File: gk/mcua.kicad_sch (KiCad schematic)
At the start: 16 parts, among them SW1 SW_Push, SW2 SW_Push, U4 STM32H747BITx, Y1 16MHz

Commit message: Update pcb
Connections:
- net SPKR_VOLUME: now also U4.45 (PA0); no longer U4.57 (PA4)
- net CTP_NRESET: now reaches U4.10 (PC13)
- net CTP_INT: now reaches U4.11 (PC14)
- net LED_BACKLIGHT_PWM: now reaches U4.149 (PA11)
- net SDMMC_DETECT: now reaches U4.166 (PA15)
- no-connect marks 26 -> 22
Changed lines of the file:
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@@
   (no_connect (at 68.58 146.05))
   (no_connect (at 71.12 146.05))
-  (no_connect (at 73.66 49.53))
-  (no_connect (at 35.56 49.53))
   (no_connect (at 99.06 146.05))
   (no_connect (at 139.7 49.53))
+  (no_connect (at 45.72 49.53))
   (no_connect (at 175.26 49.53))
   (no_connect (at 172.72 49.53))
@@
   (no_connect (at 165.1 146.05))
   (no_connect (at 63.5 146.05))
-  (no_connect (at 154.94 49.53))
   (no_connect (at 66.04 146.05))
-  (no_connect (at 63.5 49.53))
-  (no_connect (at 157.48 49.53))
   (no_connect (at 50.8 146.05))
   (no_connect (at 160.02 49.53))
@@
     )
   )
+  (global_label "CTP_INT" (shape input) (at 157.48 49.53 90) (fields_autoplaced)
+    (effects (font (size 1.27 1.27)) (justify left))
+    (property "Intersheetrefs" "${INTERSHEET_REFS}" (at 157.48 39.2461 90)
+      (effects (font (size 1.27 1.27)) (justify left) hide)
+    )
+  )
   (global_label "WIFI_CHIP_EN" (shape input) (at 195.58 49.53 90) (fields_autoplaced)
     (effects (font (size 1.27 1.27)) (justify left))
@@
     )
   )
+  (global_label "LED_BACKLIGHT_PWM" (shape input) (at 63.5 49.53 90) (fields_autoplaced)
+    (effects (font (size 1.27 1.27)) (justify left))
+    (property "Intersheetrefs" "${INTERSHEET_REFS}" (at 63.5 26.9695 90)
+      (effects (font (size 1.27 1.27)) (justify left) hide)
+    )
+  )
   (global_label "PCM_FMT" (shape input) (at 88.9 146.05 270) (fields_autoplaced)
     (effects (font (size 1.27 1.27)) (justify right))
@@
     )
   )
-  (global_label "SPKR_VOLUME" (shape input) (at 45.72 49.53 90) (fields_autoplaced)
-    (effects (font (size 1.27 1.27)) (justify left))
-    (property "Intersheetrefs" "${INTERSHEET_REFS}" (at 45.72 33.259 90)
-      (effects (font (size 1.27 1.27)) (justify left) hide)
-    )
-  )
   (global_label "FMC_BA1" (shape input) (at 170.18 146.05 270) (fields_autoplaced)
     (effects (font (size 1.27 1.27)) (justify right))
@@
     )
   )
+  (global_label "CTP_NRESET" (shape input) (at 154.94 49.53 90) (fields_autoplaced)
+    (effects (font (size 1.27 1.27)) (justify left))
+    (property "Intersheetrefs" "${INTERSHEET_REFS}" (at 154.94 35.0734 90)
+      (effects (font (size 1.27 1.27)) (justify left) hide)
+    )
+  )
   (global_label "LTDC_HYSNC" (shape input) (at 104.14 146.05 270) (fields_autoplaced)
     (effects (font (size 1.27 1.27)) (justify right))
@@
       (effects (font (size 1.27 1.27)) (justify left) hide)
     )
+  )
+  (global_label "SPKR_VOLUME" (shape input) (at 35.56 49.53 90) (fields_autoplaced)
+    (effects (font (size 1.27 1.27)) (justify left))
+    (property "Intersheetrefs" "${INTERSHEET_REFS}" (at 35.56 33.259 90)
+      (effects (font (size 1.27 1.27)) (justify left) hide)
+    )
+  )
+  (global_label "SDMMC_DETECT" (shape input) (at 73.66 49.53 90) (fields_autoplaced)
+    (effects (font (size 1.27 1.27)) (justify left))
+    (property "Intersheetrefs" "${INTERSHEET_REFS}" (at 73.66 32.2311 90)
+      (effects (font (size 1.27 1.27)) (justify left) hide)
+    )

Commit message: Update pcb
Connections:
- net LSM6DSL_INT2 is gone; now on net WIFI_IRQ: U4.162 (PI1)
- net WIFI_IRQ: no longer U4.2 (PE3)
- net NTC_MCU: now reaches U4.60 (PA7)
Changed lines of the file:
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@@
   (no_connect (at 99.06 146.05))
   (no_connect (at 139.7 49.53))
+  (no_connect (at 215.9 49.53))
   (no_connect (at 45.72 49.53))
   (no_connect (at 175.26 49.53))
@@
   (no_connect (at 60.96 146.05))
   (no_connect (at 182.88 49.53))
-  (no_connect (at 53.34 49.53))
   (no_connect (at 137.16 49.53))
   (no_connect (at 177.8 49.53))
@@
     )
   )
-  (global_label "WIFI_IRQ" (shape input) (at 215.9 49.53 90) (fields_autoplaced)
-    (effects (font (size 1.27 1.27)) (justify left))
-    (property "Intersheetrefs" "${INTERSHEET_REFS}" (at 215.9 38.7017 90)
-      (effects (font (size 1.27 1.27)) (justify left) hide)
-    )
-  )
   (global_label "BTN_MCU_R" (shape input) (at 129.54 146.05 270) (fields_autoplaced)
     (effects (font (size 1.27 1.27)) (justify right))
@@
     )
   )
-  (global_label "LSM6DSL_INT2" (shape input) (at 81.28 146.05 270) (fields_autoplaced)
-    (effects (font (size 1.27 1.27)) (justify right))
-    (property "Intersheetrefs" "${INTERSHEET_REFS}" (at 81.28 162.4419 90)
-      (effects (font (size 1.27 1.27)) (justify right) hide)
-    )
-  )
   (global_label "VDD12" (shape input) (at 27.94 85.09 180) (fields_autoplaced)
     (effects (font (size 1.27 1.27)) (justify right))
@@
     )
   )
+  (global_label "NTC_MCU" (shape input) (at 53.34 49.53 90) (fields_autoplaced)
+    (effects (font (size 1.27 1.27)) (justify left))
+    (property "Intersheetrefs" "${INTERSHEET_REFS}" (at 53.34 38.0366 90)
+      (effects (font (size 1.27 1.27)) (justify left) hide)
+    )
+  )
   (global_label "FMC_A12" (shape input) (at 162.56 146.05 270) (fields_autoplaced)
     (effects (font (size 1.27 1.27)) (justify right))
@@
     )
   )
+  (global_label "WIFI_IRQ" (shape input) (at 81.28 146.05 270) (fields_autoplaced)
+    (effects (font (size 1.27 1.27)) (justify right))
+    (property "Intersheetrefs" "${INTERSHEET_REFS}" (at 81.28 156.8783 90)
+      (effects (font (size 1.27 1.27)) (justify right) hide)
+    )
+  )

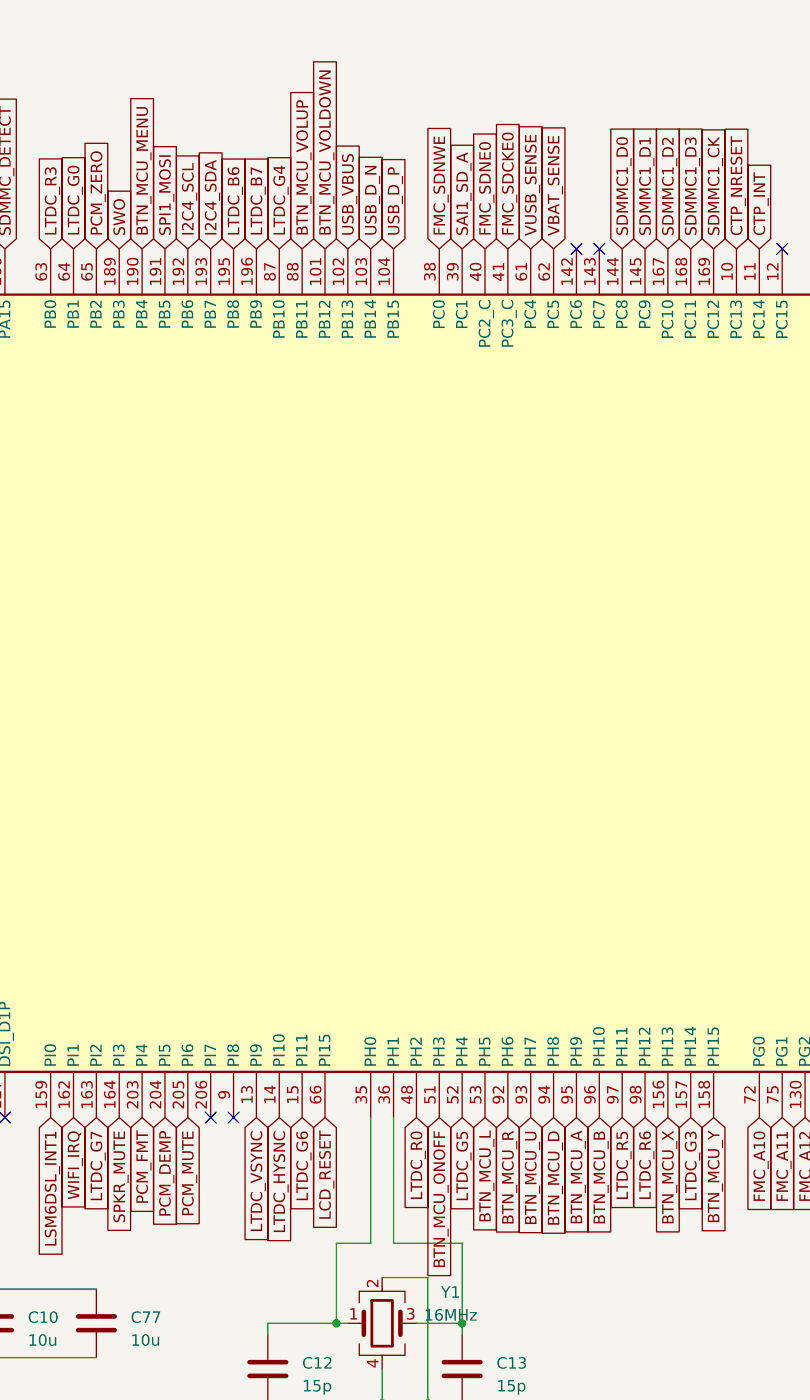
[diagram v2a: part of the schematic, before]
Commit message: Add mount pin for abxy/udlr buttons Fix button spacing Add leds for menu button
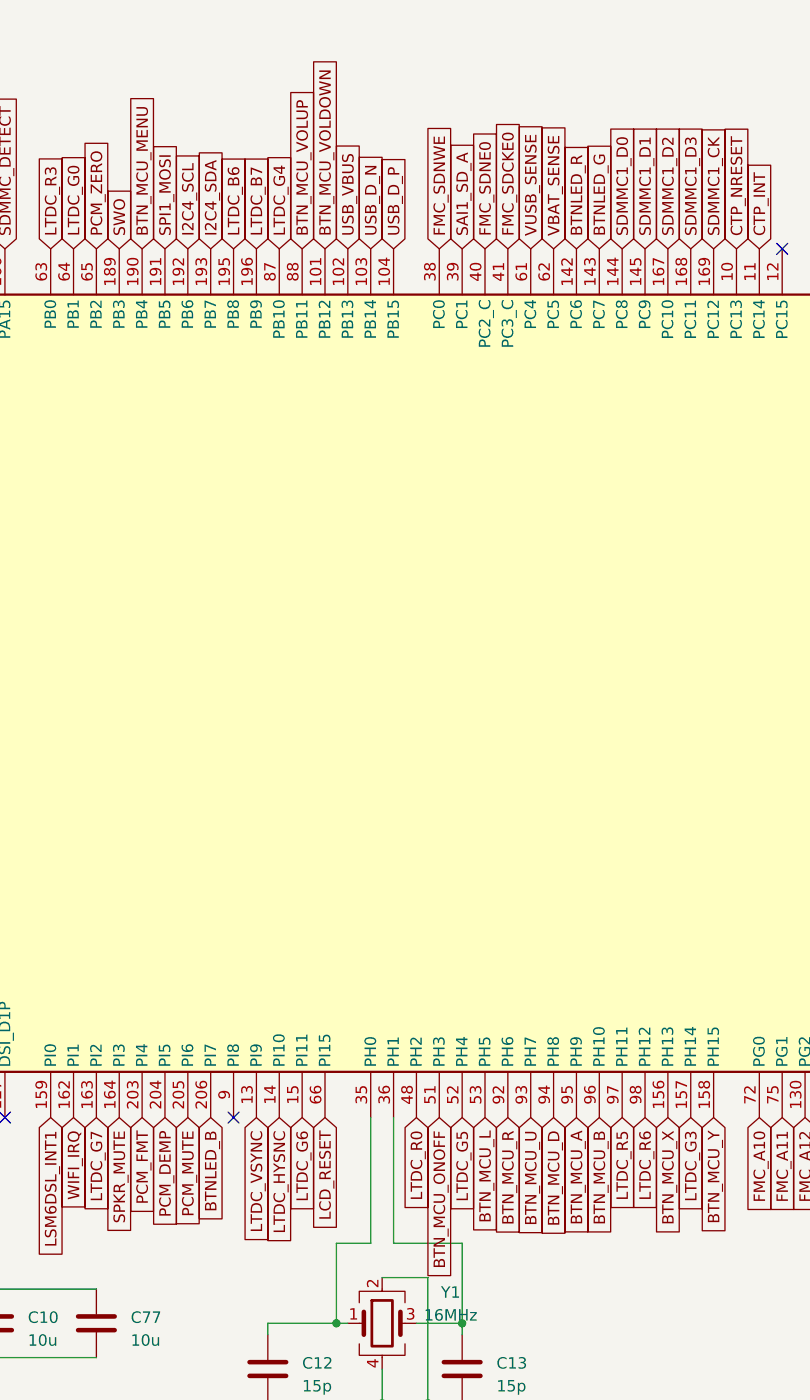
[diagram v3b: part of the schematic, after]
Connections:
- net BTNLED_R: now reaches U4.142 (PC6)
- net BTNLED_G: now reaches U4.143 (PC7)
- net BTNLED_B: now reaches U4.206 (PI7)
- no-connect marks 22 -> 19
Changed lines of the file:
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@@
   (no_connect (at 71.12 146.05))
   (no_connect (at 99.06 146.05))
-  (no_connect (at 139.7 49.53))
   (no_connect (at 215.9 49.53))
   (no_connect (at 45.72 49.53))
@@
   (no_connect (at 60.96 146.05))
   (no_connect (at 182.88 49.53))
-  (no_connect (at 137.16 49.53))
   (no_connect (at 177.8 49.53))
-  (no_connect (at 96.52 146.05))
   (wire (pts (xy 266.7 97.79) (xy 266.7 100.33))
     (stroke (width 0) (type default))
@@
     )
   )
+  (global_label "BTNLED_G" (shape input) (at 139.7 49.53 90) (fields_autoplaced)
+    (effects (font (size 1.27 1.27)) (justify left))
+    (property "Intersheetrefs" "${INTERSHEET_REFS}" (at 139.7 37.3714 90)
+      (effects (font (size 1.27 1.27)) (justify left) hide)
+    )
+  )
   (global_label "CTP_INT" (shape input) (at 157.48 49.53 90) (fields_autoplaced)
     (effects (font (size 1.27 1.27)) (justify left))
@@
     )
   )
+  (global_label "BTNLED_B" (shape input) (at 96.52 146.05 270) (fields_autoplaced)
+    (effects (font (size 1.27 1.27)) (justify right))
+    (property "Intersheetrefs" "${INTERSHEET_REFS}" (at 96.52 158.2086 90)
+      (effects (font (size 1.27 1.27)) (justify right) hide)
+    )
+  )
   (global_label "SPKR_VOLUME" (shape input) (at 35.56 49.53 90) (fields_autoplaced)
     (effects (font (size 1.27 1.27)) (justify left))
@@
     )
   )
+  (global_label "BTNLED_R" (shape input) (at 137.16 49.53 90) (fields_autoplaced)
+    (effects (font (size 1.27 1.27)) (justify left))
+    (property "Intersheetrefs" "${INTERSHEET_REFS}" (at 137.16 37.3714 90)
+      (effects (font (size 1.27 1.27)) (justify left) hide)
+    )
+  )

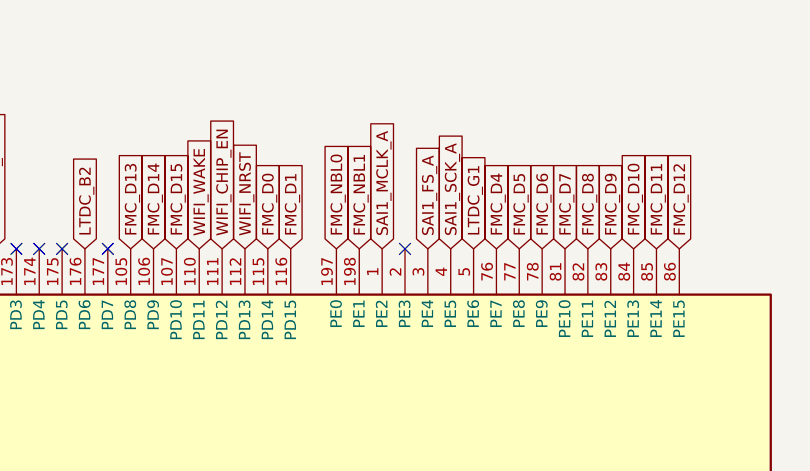
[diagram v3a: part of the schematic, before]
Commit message: Add vbat_stat detection
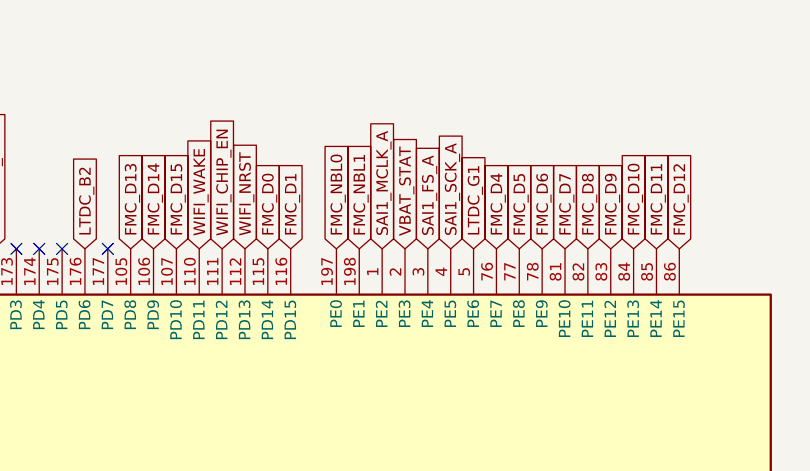
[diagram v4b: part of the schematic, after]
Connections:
- net VBAT_STAT: now reaches U4.2 (PE3)
- no-connect marks 19 -> 18
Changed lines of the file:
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@@
   (no_connect (at 71.12 146.05))
   (no_connect (at 99.06 146.05))
-  (no_connect (at 215.9 49.53))
   (no_connect (at 45.72 49.53))
   (no_connect (at 175.26 49.53))
@@
       (effects (font (size 1.27 1.27)) (justify left) hide)
     )
+  )
+  (global_label "VBAT_STAT" (shape input) (at 215.9 49.53 90) (fields_autoplaced)
+    (effects (font (size 1.27 1.27)) (justify left))
+    (property "Intersheetrefs" "${INTERSHEET_REFS}" (at 215.9 37.0085 90)
+      (effects (font (size 1.27 1.27)) (justify left) hide)
+    )

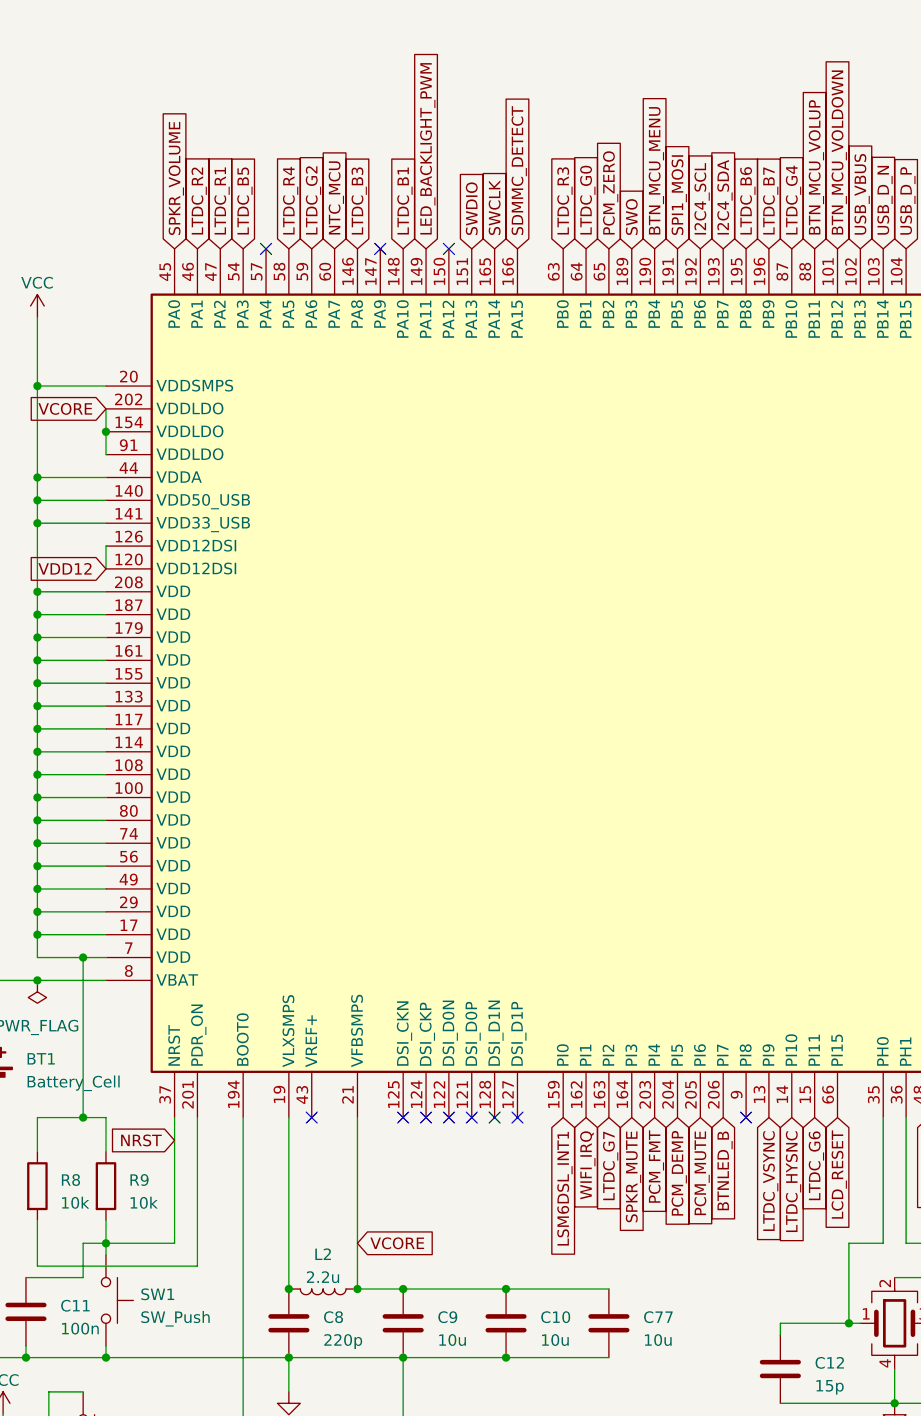
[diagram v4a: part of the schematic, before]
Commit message: Switch speaker amplifier to mono
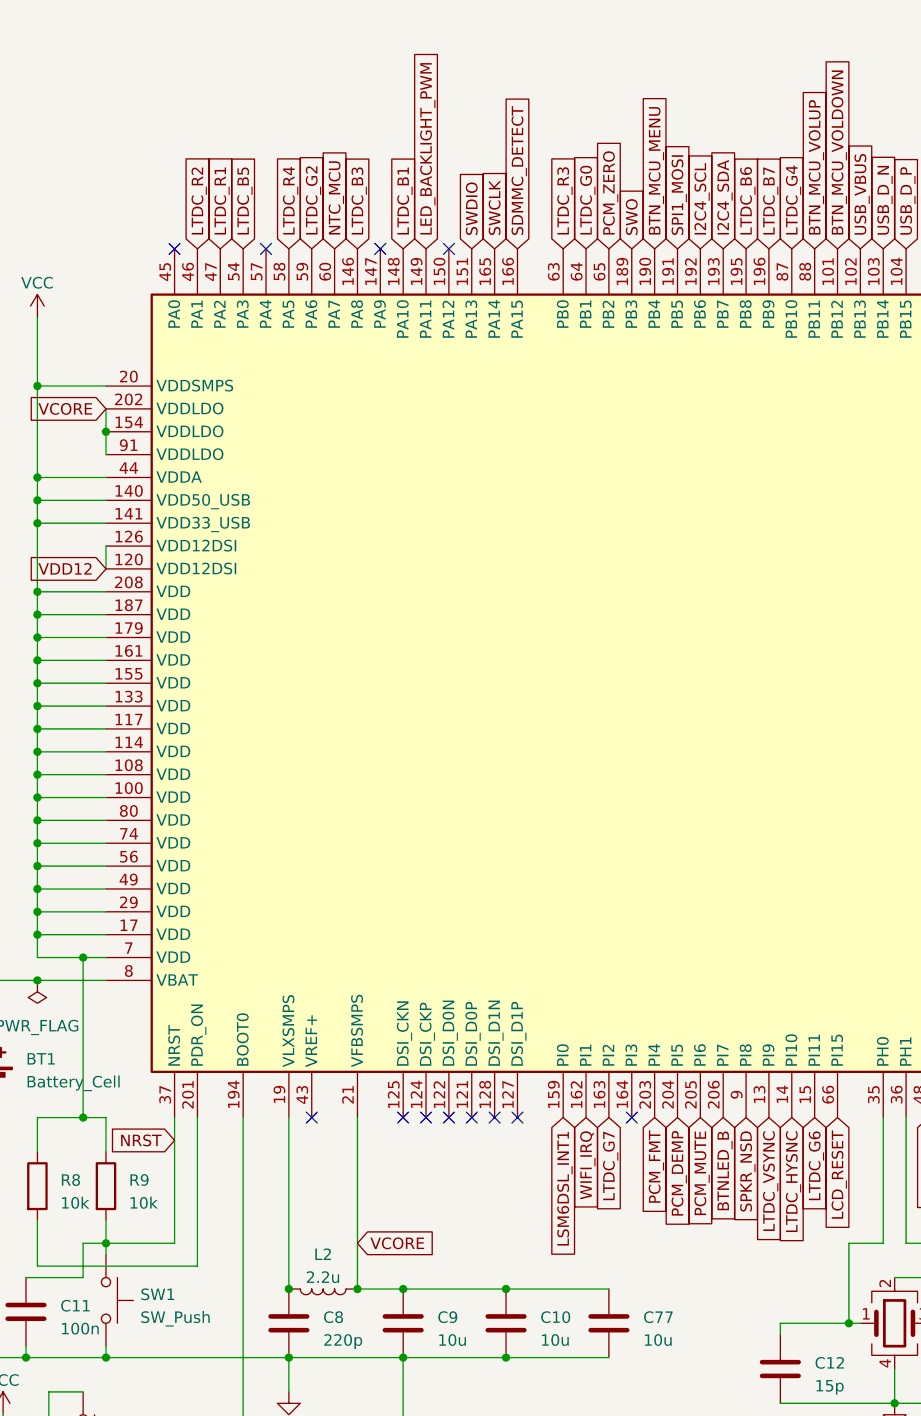
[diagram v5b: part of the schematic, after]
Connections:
- net SPKR_NSD: now reaches U4.9 (PI8)
- net SPKR_MUTE: no longer names the net of U4.164 (PI3)
- net SPKR_VOLUME: no longer names the net of U4.45 (PA0)
- no-connect marks 18 -> 19
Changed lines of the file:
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@@
   (no_connect (at 68.58 146.05))
   (no_connect (at 71.12 146.05))
-  (no_connect (at 99.06 146.05))
   (no_connect (at 45.72 49.53))
   (no_connect (at 175.26 49.53))
@@
   (no_connect (at 190.5 146.05))
   (no_connect (at 66.04 49.53))
+  (no_connect (at 35.56 49.53))
   (no_connect (at 165.1 146.05))
   (no_connect (at 63.5 146.05))
@@
   (no_connect (at 50.8 146.05))
   (no_connect (at 160.02 49.53))
+  (no_connect (at 86.36 146.05))
   (no_connect (at 73.66 146.05))
   (no_connect (at 58.42 49.53))
@@
     )
   )
-  (global_label "SPKR_MUTE" (shape input) (at 86.36 146.05 270) (fields_autoplaced)
-    (effects (font (size 1.27 1.27)) (justify right))
-    (property "Intersheetrefs" "${INTERSHEET_REFS}" (at 86.36 159.8414 90)
-      (effects (font (size 1.27 1.27)) (justify right) hide)
-    )
-  )
   (global_label "FMC_D9" (shape input) (at 238.76 49.53 90) (fields_autoplaced)
     (effects (font (size 1.27 1.27)) (justify left))
@@
     )
   )
+  (global_label "SPKR_NSD" (shape input) (at 99.06 146.05 270) (fields_autoplaced)
+    (effects (font (size 1.27 1.27)) (justify right))
+    (property "Intersheetrefs" "${INTERSHEET_REFS}" (at 99.06 158.7529 90)
+      (effects (font (size 1.27 1.27)) (justify right) hide)
+    )
+  )
   (global_label "FMC_SDNE0" (shape input) (at 127 49.53 90) (fields_autoplaced)
     (effects (font (size 1.27 1.27)) (justify left))
@@
     )
   )
-  (global_label "SPKR_VOLUME" (shape input) (at 35.56 49.53 90) (fields_autoplaced)
-    (effects (font (size 1.27 1.27)) (justify left))
-    (property "Intersheetrefs" "${INTERSHEET_REFS}" (at 35.56 33.259 90)
-      (effects (font (size 1.27 1.27)) (justify left) hide)
-    )
-  )
